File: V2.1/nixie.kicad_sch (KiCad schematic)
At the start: 66 parts, among them IC1 K155ID1, IC1 TPS54302DDCT, IC2 SN74141, IC3 K155ID1, IC4 K155ID1, IC5 MCP23017-E_SO, IC6 DS3231M+TRL, IC7 K155ID1, IC8 K155ID1, J1 M20-9990446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

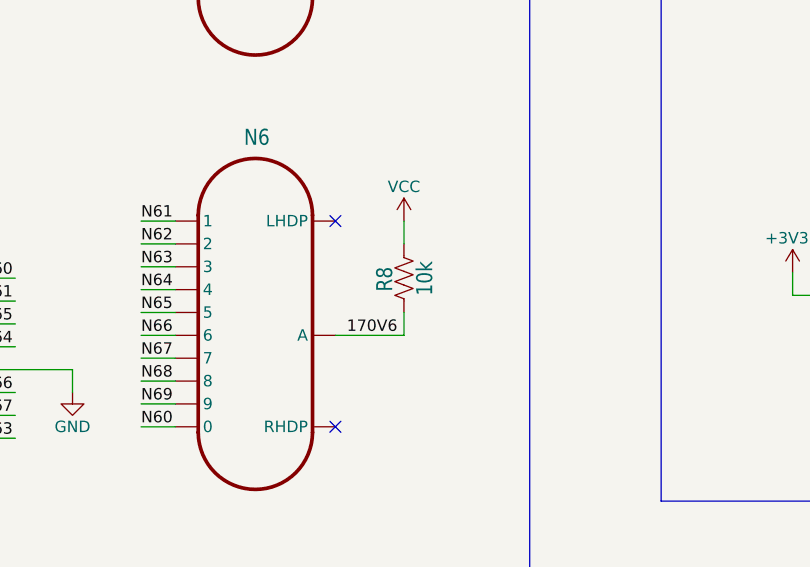
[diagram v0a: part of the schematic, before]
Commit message: Reorganizing Repo
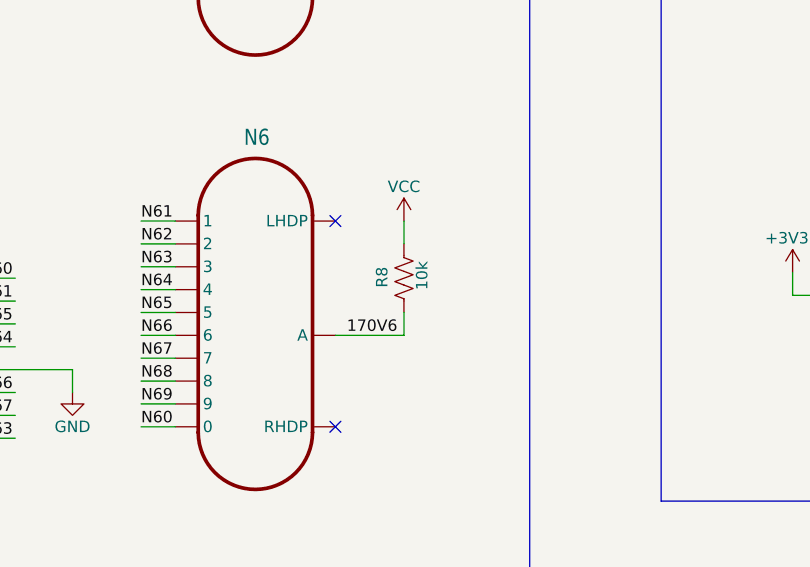
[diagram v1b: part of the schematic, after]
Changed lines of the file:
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@@
     (in_bom yes) (on_board yes) (dnp no)
     (property "Reference" "R8" (at 302.895 260.985 90)
-      (effects (font (size 1.778 1.5113)) (justify left bottom))
+      (effects (font (size 1.27 1.27)) (justify left bottom))
     )
     (property "Value" "10k" (at 307.34 260.35 90)
-      (effects (font (size 1.778 1.5113)) (justify left bottom))
+      (effects (font (size 1.27 1.27)) (justify left bottom))
     )
     (property "Footprint" "nixie:R0805" (at 305.054 262.001 90)

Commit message: Adjsuted more items in schematic, began layout
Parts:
- removed H5, H6: MountingHole, MountingHole:MountingHole_3.5mm_Pad_Via, symbol Mechanical:MountingHole
- BAT1: value SN2032 -> 36-106-ND; footprint nixie:SN2032 -> Battery:BatteryHolder_Keystone_106_1x20mm
- C1, C2, C3, C4, C5, C7, C8, C9: footprint nixie:C0805 -> Capacitor_SMD:C_0805_2012Metric
- J1: footprint Connector_PinHeader_2.54mm:PinHeader_1x04_P2.54mm_Vertical -> Connector_PinSocket_2.54mm:PinSocket_1x04_P2.54mm_Vertical
- R1, R10, R11, R2, R3, R4, R5, R6, R7, R8, R9: footprint nixie:R0805 -> Resistor_SMD:R_0805_2012Metric
- S1, S3, S4, S5, S6: footprint PTS647SN50SMTR2LFS -> footprints:PTS647SN50SMTR2LFS
- S2: footprint j2 -> footprints:PTS647SN50SMTR2LFS
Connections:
- net +12V: now also C7.1
- net +3V3: now also S3.4
- net +5V: no longer C7.1

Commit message: Started routing
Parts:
- added C11: 10uF, Capacitor_SMD:C_0805_2012Metric, symbol Device:C
- J1: footprint Connector_PinSocket_2.54mm:PinSocket_1x04_P2.54mm_Vertical -> Connector_PinHeader_2.54mm:PinHeader_1x04_P2.54mm_Vertical
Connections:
- net +5V: now also C11.1
- net GND: now also C11.2
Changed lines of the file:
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@@
     (stroke (width 0.1524) (type solid))
   )
+  (wire (pts (xy 102.235 37.465) (xy 102.235 40.005))
+    (stroke (width 0.1524) (type solid))
+  )
   (wire (pts (xy 33.02 80.01) (xy 40.64 80.01))
     (stroke (width 0) (type default))
@@
     (stroke (width 0) (type default))
   )
+  (wire (pts (xy 102.235 29.845) (xy 102.235 27.305))
+    (stroke (width 0.1524) (type solid))
+  )
   (wire (pts (xy 29.21 215.265) (xy 24.13 215.265))
     (stroke (width 0.1524) (type solid))
@@
     (fill (type none))
   )
-  (rectangle (start 26.67 19.685) (end 104.775 98.425)
+  (rectangle (start 26.67 19.685) (end 109.22 98.425)
     (stroke (width 0) (type default))
     (fill (type none))
@@
     )
   )
+  (symbol (lib_id "Device:C") (at 102.235 33.655 0) (unit 1)
+    (in_bom yes) (on_board yes) (dnp no)
+    (property "Reference" "C11" (at 102.87 32.385 0)
+      (effects (font (size 1.27 1.27)) (justify left bottom))
+    )
+    (property "Value" "10uF" (at 102.87 36.83 0)
+      (effects (font (size 1.27 1.27)) (justify left bottom))
+    )
+    (property "Footprint" "Capacitor_SMD:C_0805_2012Metric" (at 103.2002 37.465 0)
+      (effects (font (size 1.27 1.27)) hide)
+    )
+    (property "Datasheet" "~" (at 102.235 33.655 0)
+      (effects (font (size 1.27 1.27)) hide)
+    )
+    (pin "1")
+    (pin "2")
+    (instances
+      (project "nixie"
+        (path "/ba431371-aaad-4536-8520-64dab3af26c3"
+          (reference "C11") (unit 1)
+        )
+      )
+    )
+  )
   (symbol (lib_id "PTS647SN50SMTR2LFS:PTS647SN50SMTR2LFS") (at 384.175 99.06 0) (unit 1)
     (in_bom yes) (on_board yes) (dnp no)
@@
     )
   )
+  (symbol (lib_id "power:+5V") (at 102.235 27.305 0) (unit 1)
+    (in_bom yes) (on_board yes) (dnp no) (fields_autoplaced)
+    (property "Reference" "#PWR024" (at 102.235 31.115 0)
+      (effects (font (size 1.27 1.27)) hide)
+    )
+    (property "Value" "+5V" (at 102.235 23.495 0)
+      (effects (font (size 1.27 1.27)))
+    )
+    (property "Footprint" "" (at 102.235 27.305 0)
+      (effects (font (size 1.27 1.27)) hide)
+    )
+    (property "Datasheet" "" (at 102.235 27.305 0)
+      (effects (font (size 1.27 1.27)) hide)
+    )
+    (pin "1")
+    (instances
+      (project "nixie"
+        (path "/ba431371-aaad-4536-8520-64dab3af26c3"
+          (reference "#PWR024") (unit 1)
+        )
+      )
+    )
+  )
+  (symbol (lib_id "power:GND") (at 102.235 40.005 0) (unit 1)
+    (in_bom yes) (on_board yes) (dnp no)
+    (property "Reference" "#PWR074" (at 102.235 46.355 0)
+      (effects (font (size 1.27 1.27)) hide)
+    )
+    (property "Value" "GND" (at 102.235 43.815 0)
+      (effects (font (size 1.27 1.27)))
+    )
+    (property "Footprint" "" (at 102.235 40.005 0)
+      (effects (font (size 1.27 1.27)) hide)
+    )
+    (property "Datasheet" "" (at 102.235 40.005 0)
+      (effects (font (size 1.27 1.27)) hide)
+    )
+    (pin "1")
+    (instances
+      (project "nixie"
+        (path "/ba431371-aaad-4536-8520-64dab3af26c3"
+          (reference "#PWR074") (unit 1)
+        )
+      )
+    )
+  )
   (symbol (lib_id "TimeExpander:K155ID1_") (at 29.21 252.095 0) (unit 1)
     (in_bom yes) (on_board yes) (dnp no)
@@
       (effects (font (size 1.27 1.27)) (justify left) hide)
     )
-    (property "Footprint" "Connector_PinSocket_2.54mm:PinSocket_1x04_P2.54mm_Vertical" (at 363.22 266.7 0)
+    (property "Footprint" "Connector_PinHeader_2.54mm:PinHeader_1x04_P2.54mm_Vertical" (at 363.22 266.7 0)
       (effects (font (size 1.27 1.27)) hide)
     )

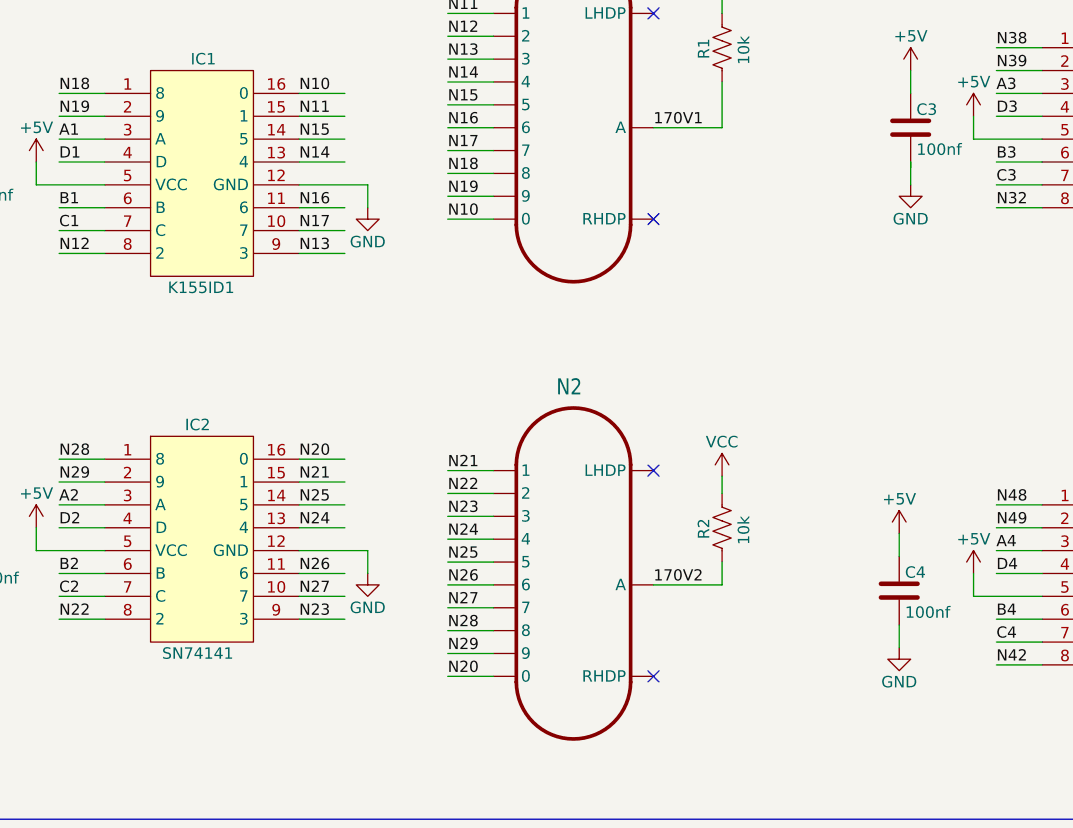
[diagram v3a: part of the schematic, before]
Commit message: Updated bom, slightchanges to footprint indicators
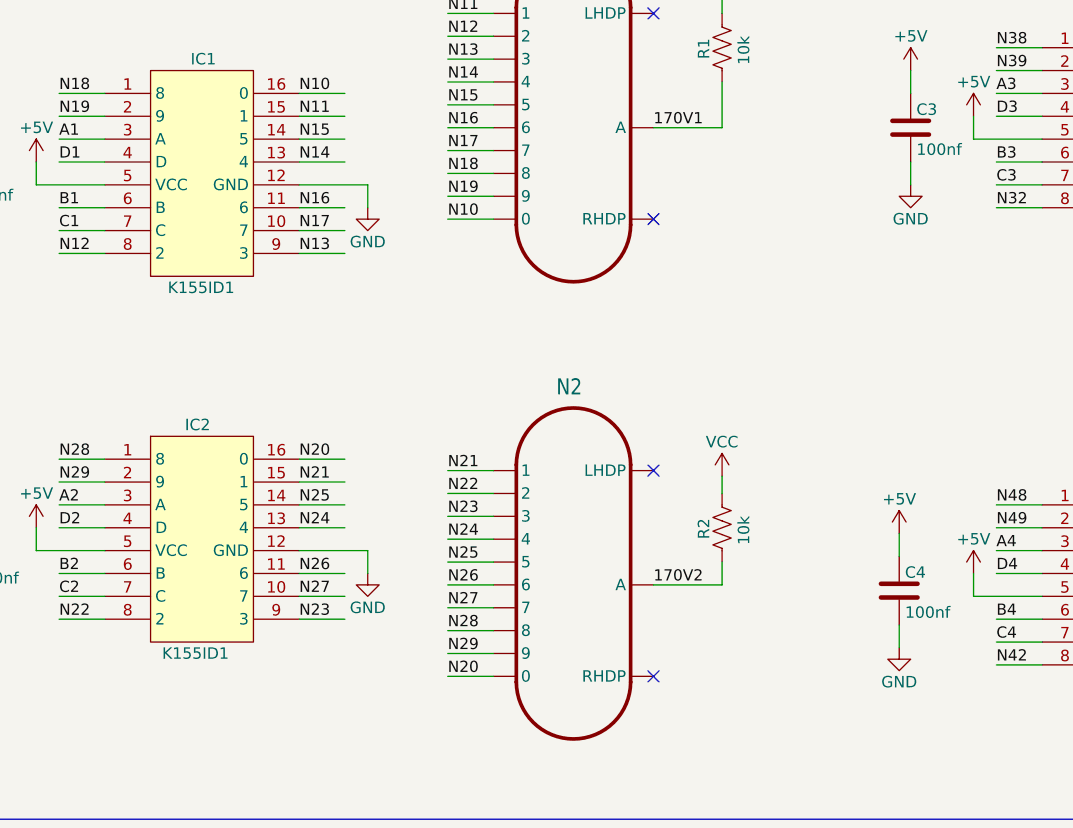
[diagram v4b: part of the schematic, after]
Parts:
- IC2: value SN74141 -> K155ID1
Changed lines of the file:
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@@
     (stroke (width 0.1524) (type solid))
   )
-  (wire (pts (xy 118.745 222.885) (xy 118.745 223.52))
-    (stroke (width 0) (type default))
-  )
   (wire (pts (xy 154.94 222.885) (xy 160.02 222.885))
     (stroke (width 0.1524) (type solid))
@@
     (stroke (width 0.1524) (type solid))
   )
+  (wire (pts (xy 118.745 222.885) (xy 118.745 225.425))
+    (stroke (width 0) (type default))
+  )
   (wire (pts (xy 133.35 266.065) (xy 128.27 266.065))
     (stroke (width 0.1524) (type solid))
@@
     (stroke (width 0.1524) (type solid))
   )
-  (wire (pts (xy 118.745 222.885) (xy 118.745 225.425))
-    (stroke (width 0.1524) (type solid))
-  )
   (wire (pts (xy 50.8 255.905) (xy 55.88 255.905))
     (stroke (width 0.1524) (type solid))
@@
       (project "nixie"
         (path "/ba431371-aaad-4536-8520-64dab3af26c3"
-          (reference "IC10") (unit 1)
+          (reference "IC9") (unit 1)
         )
       )
@@
       (effects (font (size 1.27 1.27)) hide)
     )
-    (property "Datasheet" "105 kOhms ±1% 0.25W, 1/4W Chip Resistor 0805 (2012 Metric) Automotive AEC-Q200, Moisture Resistant Thick Film" (at 271.78 60.325 0)
+    (property "Datasheet" "https://www.digikey.com/en/products/detail/koa-speer-electronics-inc/RK73H2ATTD1053F/10234720" (at 271.78 60.325 0)
       (effects (font (size 1.27 1.27)) hide)
     )
@@
       (project "nixie"
         (path "/ba431371-aaad-4536-8520-64dab3af26c3"
-          (reference "C18") (unit 1)
+          (reference "C17") (unit 1)
         )
       )
@@
       (effects (font (size 1.27 1.27)) (justify left))
     )
-    (property "Value" "SN74141" (at 35.56 277.495 0)
+    (property "Value" "K155ID1" (at 35.56 277.495 0)
       (effects (font (size 1.27 1.27)) (justify left))
     )
